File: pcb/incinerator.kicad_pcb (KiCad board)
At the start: 2 copper layers, 73.7 x 76.8 mm, 51 parts, among them J1 Power Source 12V, J2 IGNITION_MAIN, J3 IGNITION_AFT, J4 VALVE_MAIN, J5 VALVE_AFT_HI, J6 VALVE_AFT_LO, J7 AIRPMP, J8 To encoder, J9 To e-paper, Q1 IRLU120N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

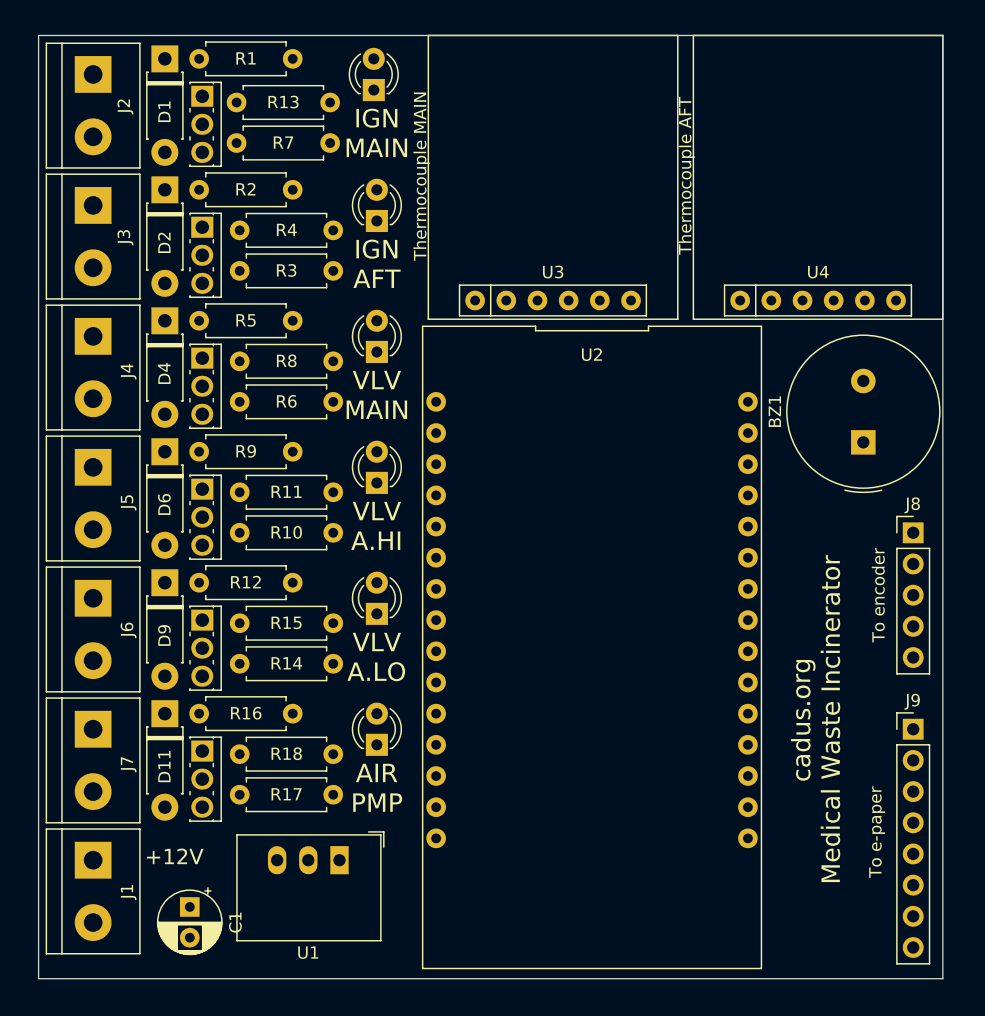
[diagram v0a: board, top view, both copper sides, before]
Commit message: added traces & ground planes
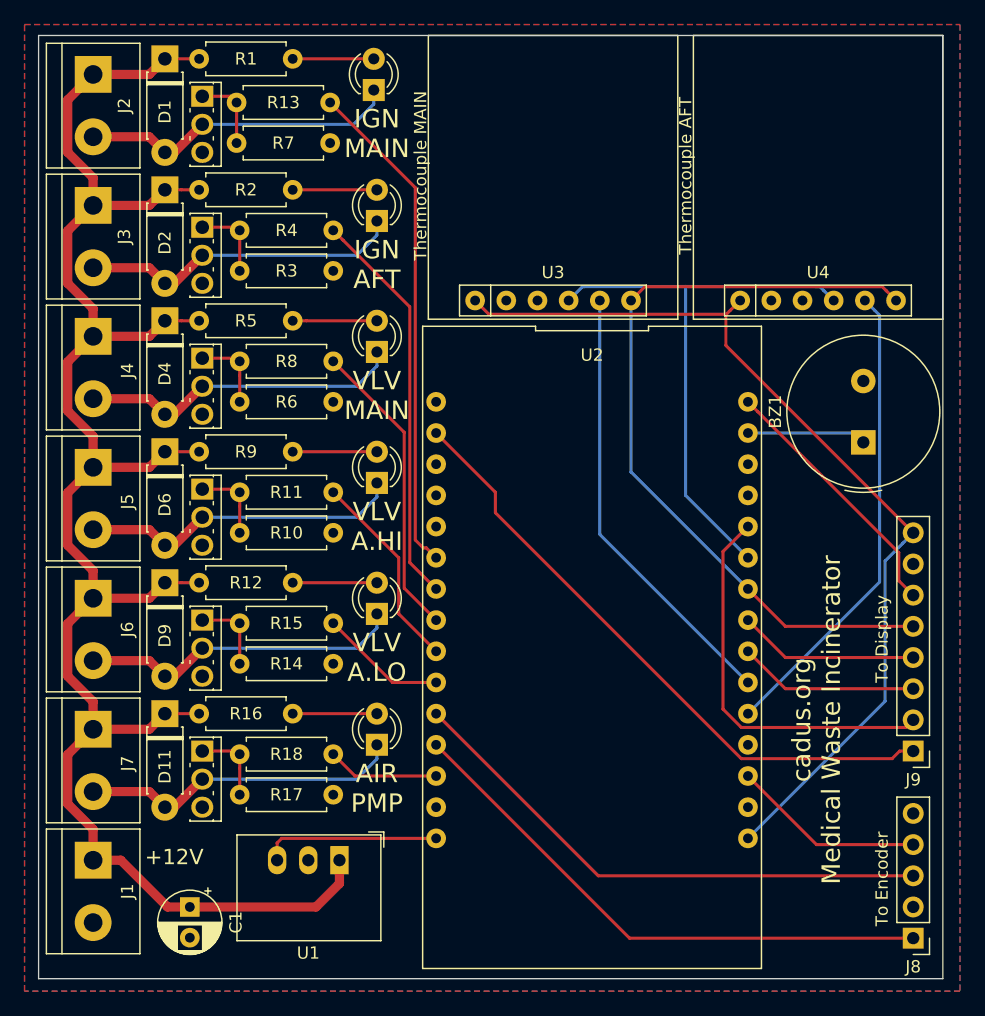
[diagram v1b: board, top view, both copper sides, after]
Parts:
- J8: value To encoder -> To Encoder
- J9: value To e-paper -> To Display
- U3, U4: value Adafruit MAX31855 -> Adafruit_MAX31855
- moved J8 33.0 mm to (172.7, 124.0), turned to 180 degrees
- moved J9 1.78 mm to (172.7, 108.7), turned to 180 degrees
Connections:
- U2 pad 11: /ROT_DT -> /ROT_CLK
- U2 pad 12: /ROT_CLK -> /ROT_DT
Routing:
- net +12V: track 0.00 -> 153.6 mm
- net +3V3: track 0.00 -> 77.1 mm
- net /CLK: track 0.00 -> 64.9 mm
- net /BUSY: track 0.00 -> 51.1 mm
- net Net-(U2-Pad25): track 0.00 -> 47.5 mm
- net /ROT_DT: track 0.00 -> 45.4 mm
- net /ROT_CLK: track 0.00 -> 44.3 mm
- net Net-(R13-Pad2): track 0.00 -> 40.8 mm
- net Net-(U2-Pad20): track 0.00 -> 38.6 mm
- net Net-(U2-Pad21): track 0.00 -> 36.3 mm
- net Net-(R4-Pad2): track 0.00 -> 32.7 mm
- net /RST: track 0.00 -> 32.1 mm
- net Net-(D11-Pad2): track 0.00 -> 26.4 mm
- net Net-(D6-Pad2): track 0.00 -> 26.4 mm
- net Net-(D2-Pad2): track 0.00 -> 26.4 mm
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- added copper zone on B.Cu, net Earth
- added copper zone on F.Cu, net Earth
